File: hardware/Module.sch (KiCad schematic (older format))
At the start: 92 parts, among them J1 Power, J10 Jack, J11 A I/O, J12 Debug, J13 A IFACE, J2 B IFACE, J3 B I/O, J4 Jack, J5 Jack, J6 Jack, J7 Jack, J8 Jack, J9 Jack, SW2 Button, U1 MCP6004, U4 LM4040C10, U6 TL072, U9 MCP6002

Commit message: Prepare the schematic
Signed-off-by: Petr Horacek <hrck@protonmail.com>
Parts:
- removed C35, C37: 1n, Capacitor_SMD:C_0603_1608Metric_Pad1.08x0.95mm_HandSolder, symbol Device:C_Small
- removed D10, D3, D4, D5, D6, D7, D8, D9: LED, LED_THT:LED_D3.0mm, symbol Device:LED_Small
- removed J11: A I/O, Connector_PinHeader_2.54mm:PinHeader_2x06_P2.54mm_Vertical, symbol Connector_Generic:Conn_02x06_Odd_Even
- removed J13: A IFACE, Connector_PinHeader_2.54mm:PinHeader_2x08_P2.54mm_Vertical, symbol Connector_Generic:Conn_02x08_Odd_Even
- removed J2: B IFACE, Connector_PinSocket_2.54mm:PinSocket_2x08_P2.54mm_Vertical, symbol Connector_Generic:Conn_02x08_Odd_Even
- removed J3: B I/O, Connector_PinSocket_2.54mm:PinSocket_2x06_P2.54mm_Vertical, symbol Connector_Generic:Conn_02x06_Odd_Even
- removed R36, R37, R40, R41: 1k, Resistor_SMD:R_0603_1608Metric_Pad0.98x0.95mm_HandSolder, symbol Device:R_Small
- removed R50, R51: 47k, Resistor_SMD:R_0603_1608Metric_Pad0.98x0.95mm_HandSolder, symbol Device:R_Small
- removed RV1, RV2, RV3, RV4: B10k, Potentiometer_THT:Potentiometer_Alpha_RD901F-40-00D_Single_Vertical, symbol Device:R_POT
- removed SW2: Button, Button_Switch_THT:SW_PUSH_6mm, symbol Switch:SW_Push
- removed U6: TL072, Package_SO:SOIC-8_3.9x4.9mm_P1.27mm, symbol Amplifier_Operational:TL072
- added C1, C6, C7, C8, C9: 100n, Capacitor_SMD:C_0603_1608Metric_Pad1.08x0.95mm_HandSolder, symbol Device:C_Small
- added C2, C3: 18p, Capacitor_SMD:C_0603_1608Metric_Pad1.08x0.95mm_HandSolder, symbol Device:C_Small
- added D1: Schottky, Diode_SMD:D_SOD-123, symbol Device:D_Schottky_Small
- added J1, J4: Jack, symbol Connector:AudioJack3
- added J10, J5, J6, J7, J8, J9: Jack, Connector_Audio:Jack_3.5mm_QingPu_WQP-PJ398SM_Vertical_CircularHoles, symbol Connector:AudioJack2_SwitchT
- added J13: Micro_SD, symbol Connector:Micro_SD_Card
- added J2: OLED, symbol Connector_Generic:Conn_01x04
- added R1: 33R, Resistor_SMD:R_0603_1608Metric_Pad0.98x0.95mm_HandSolder, symbol Device:R_Small
- added R10, R14, R15, R20, R21, R26, R27, R28, R29: 100k, Resistor_SMD:R_0603_1608Metric_Pad0.98x0.95mm_HandSolder, symbol Device:R_Small
- added R12, R13: 6k8, Resistor_SMD:R_0603_1608Metric_Pad0.98x0.95mm_HandSolder, symbol Device:R_Small
- added R16, R17: 200k, Resistor_SMD:R_0603_1608Metric_Pad0.98x0.95mm_HandSolder, symbol Device:R_Small
- added R18, R19, R34: 1k, Resistor_SMD:R_0603_1608Metric_Pad0.98x0.95mm_HandSolder, symbol Device:R_Small
- added R2: 220R, Resistor_SMD:R_0603_1608Metric_Pad0.98x0.95mm_HandSolder, symbol Device:R_Small
- added R22, R23, R24, R25, R8, R9: 33k, Resistor_SMD:R_0603_1608Metric_Pad0.98x0.95mm_HandSolder, symbol Device:R_Small
- added R3: 10R, Resistor_SMD:R_0603_1608Metric_Pad0.98x0.95mm_HandSolder, symbol Device:R_Small
- added R32, R33: 100R, Resistor_SMD:R_0603_1608Metric_Pad0.98x0.95mm_HandSolder, symbol Device:R_Small
- added R43, R44, R6: 47k, Resistor_SMD:R_0603_1608Metric_Pad0.98x0.95mm_HandSolder, symbol Device:R_Small
- added R47, R5: 10k, Resistor_SMD:R_0603_1608Metric_Pad0.98x0.95mm_HandSolder, symbol Device:R_Small
- added SW1, SW2: Encoder, Rotary_Encoder:RotaryEncoder_Alps_EC11E-Switch_Vertical_H20mm, symbol Device:Rotary_Encoder_Switch
- added U1, U2, U3: TL074, symbol Amplifier_Operational:TL074
- R11: value 2k2 -> 100k
- R35: LCSC C23032 -> C21190; Mfr Part Number CR0603-FX-3650ELF -> CR0603-FX-1001ELF
- R38, R39, R42: value 1k -> 47k; LCSC C23032 -> C25744; Mfr Part Number CR0603-FX-3650ELF -> CR0603-FX-1002ELF
- R48: renamed from R20; value 100k -> 200k
- R52: renamed from R23; value 100k -> 200k
- R59: renamed from R17; value 100k -> 200k
- R7: value 2k2 -> 47k
- renumbered C33 to C10, C34 to C11, C41 to C12, C43 to C13, C44 to C14, C46 to C15, C48 to C16, C40 to C17, C42 to C18, C38 to C4, C36 to C5, D11 to D2, D1 to D3, D2 to D4, J5 to J11, J4 to J12, J6 to J14, J8 to J15, J10 to J16, J1 to J17, J7 to J18, J9 to J19, J12 to J3, R12 to R30, R8 to R31, R13 to R36, R9 to R37, R48 to R4, R14 to R40, R10 to R41, R43 to R45, R21 to R49, R27 to R50, R28 to R51, R30 to R53, R22 to R54, R29 to R55, R31 to R56, R45 to R57, R47 to R58, R18 to R60, R24 to R61, R25 to R62, R4 to R63, R19 to R64, R26 to R65, R5 to R66, U1 to U4, U9 to U5, U9 to U6, U4 to U7
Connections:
- net A_LED4 is gone; now on net +3V3: R38.1
- net A_LED5 is gone; now on net +3V3: R39.1
- net A_LED8 is gone; now on net +3V3: R42.1
- net B_CV1_IN is gone; now on an unnamed net: R49.1
- net B_CV2_IN is gone; now on an unnamed net: R60.1
- net B_CV3_IN is gone; now on an unnamed net: R51.1
- net B_CV4_IN is gone; now on an unnamed net: R62.1
- net B_CV5_IN is gone; now on an unnamed net: R53.1
- net B_LED3 is gone; now on net SD_CMD: A1.6 (SDMMC1_CMD)
- net B_LED4 is gone; now on net SD_D0: A1.5 (SDMMC1_D0)
- net B_LED5 is gone; now on net SD_D1: A1.4 (SDMMC1_D1)
- net B_OUT1_MAIN is gone; now on an unnamed net: C5.1, R37.2
- net B_OUT2_MAIN is gone; now on an unnamed net: C4.1, R36.2
- net B_POT3 is gone; now on net DAC2: A1.30 (DAC1_OUT1)
- net B_POT4 is gone; now on net DAC1: A1.29 (DAC1_OUT2)
- net +3.3VA: now also R22.1, R24.1
- net +3V3: now also C1.1, J13.4 (VDD), J2.1 (Pin_1), R1.1, R43.1, R44.1, U1.6 (VDD)
- net DAC1: now also R11.1, R10.1; no longer A1.18 (AUDIO_OUT_L), R7.1
- net DAC2: no longer A1.19 (AUDIO_OUT_R), R11.1
- net GND: now also C1.2, C8.2, C9.1, J1.S, J10.S, J13.6 (VSS), J13.9 (SHIELD), J2.2 (Pin_2), J4.S, J5.S, J6.S, J7.S, J8.S, J9.S, SW1.C, SW1.S2, SW2.C, SW2.S2, U1.10 (+), U1.12 (+), U1.3 (+), U1.4 (GND), U1.5 (+), U2.10 (+), U2.12 (+), U2.3 (+), U2.5 (+), U3.10 (+), U3.12 (+), U3.3 (+), U3.5 (+); no longer A1.12 (I2C1_SCL), A1.13 (I2C1_SDA), A1.14 (USART1_TX), A1.15 (USART1_RX)
- net GPIO1: no longer A1.34 (SAI2_FS_B)
- net GPIO2: no longer A1.35 (SAI2_SCK_B)
- net GPIO3: no longer A1.36 (USB_HS_D_-)
- net GPIO4: no longer A1.37 (USB_HS_D_+)
- net VCC: now also C6.1, C8.1, U1.4 (V+), U2.4 (V+), U3.4 (V+)
- net VEE: now also C7.2, C9.2, U1.11 (V-), U2.11 (V-), U3.11 (V-)
- net AUDIO_IN1: now reaches A1.16 (AUDIO_IN_L)
- net AUDIO_IN1: now also R19.2
- net AUDIO_IN2: now reaches A1.17 (AUDIO_IN_R)
- net AUDIO_IN2: now also R18.2
- net ENC1_A: now reaches A1.31 (SAI2_MCLK_B)
- net ENC1_A: now also SW1.A
- net ENC1_B: now reaches A1.32 (SAI2_SD_B)
- net ENC1_B: now also SW1.B
- net ENC2_A: now reaches A1.33 (SAI2_SD_A)
- net ENC2_A: now also SW2.A
- net at R35.2: now also J10.T
- net SD_D1: now reaches R38.2
- net SD_D1: now also J13.8 (DAT1)
- net SD_D0: now reaches R39.2
- net SD_D0: now also J13.7 (DAT0)
- net SD_CMD: now reaches R42.2
- net SD_CMD: now also J13.3 (CMD)
- net at R7.2: now also C3.2, R13.1, U3.2 (-); no longer R31.1
- net at R11.2: now also R17.1, U2.2 (-); no longer R30.1
- net at J16.TN: now also R47.2; no longer R4.2
- net A_CV1_IN: no longer names the net of J14.T
- net A_CV2_IN: no longer names the net of J18.T
- net A_CV3_IN: no longer names the net of J15.T
- net A_CV4_IN: no longer names the net of J19.T
- net A_CV5_IN: no longer names the net of J16.T
- net A_LED1: no longer names the net of R35.1
- net A_LED1: now also R29.2, U2.7
- net A_OUT1_MAIN: no longer names the net of R41.1
- net A_OUT1_MAIN: now also U3.8
- net A_OUT2_MAIN: no longer names the net of R40.1
- net A_OUT2_MAIN: now also U3.14
- net A_PROBE renamed PROBE
- net PROBE: now also D2.3, R47.1, R5.1
- net B_BUTTON renamed ENC2_CLICK
- net ENC2_CLICK: now also SW2.S1
- net B_LED1 renamed ENC1_CLICK
- net ENC1_CLICK: now also SW1.S1
- net B_LED2 renamed SD_CK
- net SD_CK: now also J13.5 (CLK)
- net B_LED6 renamed SD_D2
- net SD_D2: now also J13.1 (DAT2), R44.2
- net B_LED7 renamed SD_D3
- net SD_D3: now also J13.2 (DAT3/CD), R43.2
- net B_LED8: no longer names the net of A1.1 (USB_HS_ID)
- net B_OUT1_FALL: no longer names the net of C4.2, R30.2, R36.1
- net B_OUT1_FALL: now also U3.13 (-)
- net B_OUT2_FALL: no longer names the net of C5.2, R31.2, R37.1
- net B_OUT2_FALL: now also U3.9 (-)
- net B_POT1 renamed MIDI_OUT
- net MIDI_OUT: now also R3.1
- net B_POT2 renamed MIDI_IN
- net MIDI_IN: now also U1.5 (VO)
- net B_PROBE: no longer names the net of A1.11 (SPI1_MOSI)
- net B_PROBE: no longer D2.3
- new net: J5.TN, R4.2
- new net: R14.2, R20.1, U1.1
- new net: R20.2, R26.1, U1.6 (-)
- new net: R26.2, R32.1, U1.7
- new net: J7.T, R32.2
- new net: J4.R, R1.2
- new net: J4.T, R3.2
- new net: R15.2, R21.1, U1.8
- new net: R21.2, R27.1, U1.13 (-)
- new net: R27.2, R33.1, U1.14
- new net: J8.T, R33.2
- new net: R15.1, R9.2, U1.9 (-)
- new net: R14.1, R8.2, U1.2 (-)
- new net: C6.2, C7.1
- new net: C2.1, R12.2, R18.1, U3.7
- new net: J5.T, R6.1
- new net: C2.2, R12.1, R6.2, U3.6 (-)
- new net: C3.1, R13.2, R19.1, U3.1
- new net: J6.T, R7.1
- new net: J6.TN, R5.2
- new net: R17.2, R25.1, U2.1
- new net: R24.2, R25.2, R29.1, U2.6 (-)
- new net: J9.T, R34.2
- new net: R28.2, R34.1, U2.14
- new net: R22.2, R23.2, R28.1, U2.13 (-)
- new net: R16.2, R23.1, U2.8
- new net: R10.2, R16.1, U2.9 (-)
- new net: J1.R, R2.1
- new net: D1.2 (A), J1.T, U1.3 (K)
- new net: D1.1 (K), R2.2, U1.1 (A)
- new net AUDIO_OUT1: A1.18 (AUDIO_OUT_L), R31.1
- new net AUDIO_OUT2: A1.19 (AUDIO_OUT_R), R30.1
- new net ENC2_B: A1.34 (SAI2_FS_B), SW2.B
- new net GATE1: R8.1
- new net GATE2: R9.1
- new net OLED_SCL: A1.12 (I2C1_SCL), J2.3 (Pin_3)
- new net OLED_SDA: A1.13 (I2C1_SDA), J2.4 (Pin_4)
- no-connect marks 9 -> 3
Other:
- note removed: "0.0 to 10.0"
- note removed: "Audio Output"
- note removed: "CV Input"
- note removed: "Core"
- note removed: "Display"
- note removed: "Power"
- note removed: "R17 to R31 should be 1% for best CV accuracy"
- note removed: "User Input"
- note removed: "compatibility version 0"
- moved on the sheet: C10, C11, C12, C13, C14, C15, C16, C17, C18, C19, C20, C21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

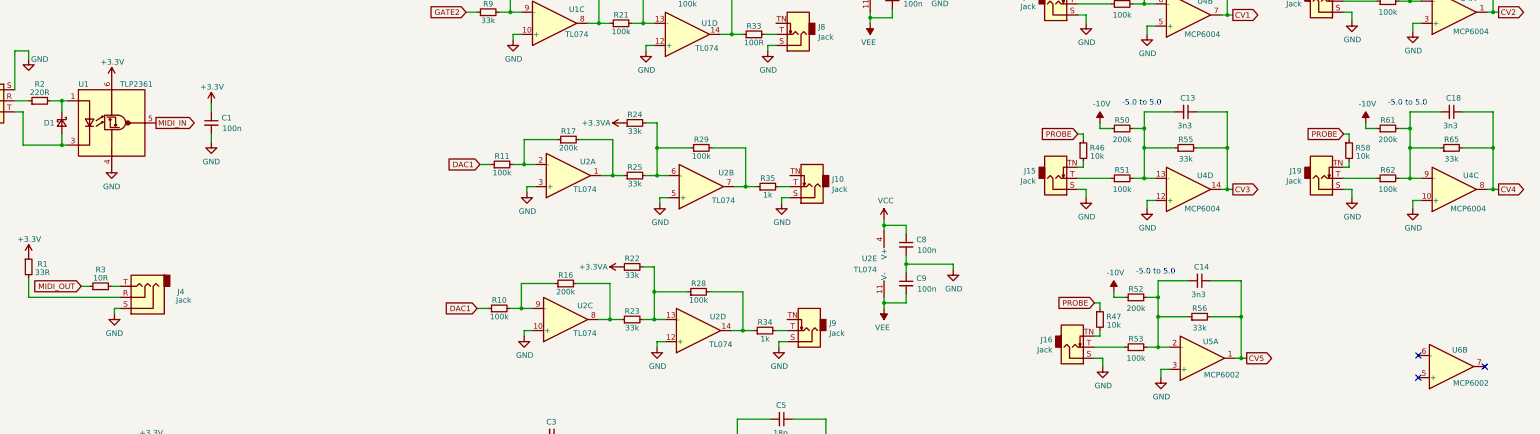
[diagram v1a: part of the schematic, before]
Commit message: Add SD card footprint
Signed-off-by: Petr Horacek <hrck@protonmail.com>
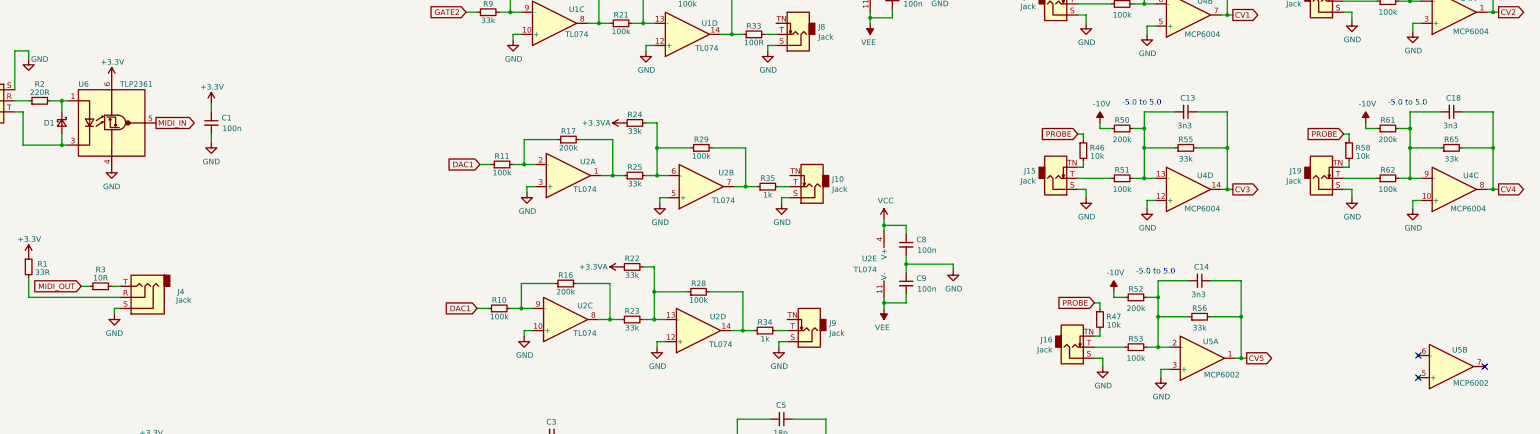
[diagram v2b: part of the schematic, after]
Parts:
- J1, J4: footprint (none) -> Connector_Audio:Jack_3.5mm_QingPu_WQP-PJ398SM_Vertical_CircularHoles
- J13: footprint (none) -> Custom:microsd_connector
- J2: footprint (none) -> Connector_PinHeader_2.54mm:PinHeader_1x04_P2.54mm_Vertical
- U1, U2, U3: footprint (none) -> Package_SO:SOIC-14_3.9x8.7mm_P1.27mm
- renumbered U6 to U5, U1 to U6
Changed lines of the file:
@@
 NoConn ~ 14825 8000
 $Comp
-L Amplifier_Operational:MCP6002-xSN U6
+L Amplifier_Operational:MCP6002-xSN U5
 U 2 1 62469350
 P 15125 7900
-F 0 "U6" H 15200 7750 50  0000 C CNN
+F 0 "U5" H 15200 7750 50  0000 C CNN
 F 1 "MCP6002" H 15300 8050 50  0000 C CNN
 F 2 "Package_SO:SOIC-8_3.9x4.9mm_P1.27mm" H 15125 7900 50  0001 C CNN
@@
 F 0 "J13" H 11125 2667 50  0000 C CNN
 F 1 "Micro_SD" H 11125 2576 50  0000 C CNN
-F 2 "" H 12325 2250 50  0001 C CNN
+F 2 "Custom:microsd_connector" H 12325 2250 50  0001 C CNN
 F 3 "http://katalog.we-online.de/em/datasheet/693072010801.pdf" H 11175 1950 50  0001 C CNN
 	1    11175 1950
@@
 F 0 "U1" H 7225 4675 50  0000 C CNN
 F 1 "TL074" H 7225 4900 50  0000 C CNN
-F 2 "" H 6975 4900 50  0001 C CNN
+F 2 "Package_SO:SOIC-14_3.9x8.7mm_P1.27mm" H 6975 4900 50  0001 C CNN
 F 3 "http://www.ti.com/lit/ds/symlink/tl071.pdf" H 7075 5000 50  0001 C CNN
 	3    7025 4800
@@
 F 0 "U1" H 8425 4800 50  0000 C CNN
 F 1 "TL074" H 8400 5025 50  0000 C CNN
-F 2 "" H 8175 5000 50  0001 C CNN
+F 2 "Package_SO:SOIC-14_3.9x8.7mm_P1.27mm" H 8175 5000 50  0001 C CNN
 F 3 "http://www.ti.com/lit/ds/symlink/tl071.pdf" H 8275 5100 50  0001 C CNN
 	4    8225 4900
@@
 F 0 "U1" H 9675 4450 50  0000 L CNN
 F 1 "TL074" H 9600 4350 50  0000 L CNN
-F 2 "" H 9925 4500 50  0001 C CNN
+F 2 "Package_SO:SOIC-14_3.9x8.7mm_P1.27mm" H 9925 4500 50  0001 C CNN
 F 3 "http://www.ti.com/lit/ds/symlink/tl071.pdf" H 10025 4600 50  0001 C CNN
 	5    9975 4400
@@
 F 0 "U1" H 7200 3700 50  0000 C CNN
 F 1 "TL074" H 7175 3950 50  0000 C CNN
-F 2 "" H 6975 3925 50  0001 C CNN
+F 2 "Package_SO:SOIC-14_3.9x8.7mm_P1.27mm" H 6975 3925 50  0001 C CNN
 F 3 "http://www.ti.com/lit/ds/symlink/tl071.pdf" H 7075 4025 50  0001 C CNN
 	1    7025 3825
@@
 F 0 "U1" H 8450 3800 50  0000 C CNN
 F 1 "TL074" H 8425 4050 50  0000 C CNN
-F 2 "" H 8175 4025 50  0001 C CNN
+F 2 "Package_SO:SOIC-14_3.9x8.7mm_P1.27mm" H 8175 4025 50  0001 C CNN
 F 3 "http://www.ti.com/lit/ds/symlink/tl071.pdf" H 8275 4125 50  0001 C CNN
 	2    8225 3925
@@
 F 0 "U3" H 7200 9075 50  0000 C CNN
 F 1 "TL074" H 7225 9300 50  0000 C CNN
-F 2 "" H 6950 9300 50  0001 C CNN
+F 2 "Package_SO:SOIC-14_3.9x8.7mm_P1.27mm" H 6950 9300 50  0001 C CNN
 F 3 "http://www.ti.com/lit/ds/symlink/tl071.pdf" H 7050 9400 50  0001 C CNN
 	1    7000 9200
@@
 F 0 "U3" H 7150 10475 50  0000 C CNN
 F 1 "TL074" H 7175 10700 50  0000 C CNN
-F 2 "" H 6925 10675 50  0001 C CNN
+F 2 "Package_SO:SOIC-14_3.9x8.7mm_P1.27mm" H 6925 10675 50  0001 C CNN
 F 3 "http://www.ti.com/lit/ds/symlink/tl071.pdf" H 7025 10775 50  0001 C CNN
 	2    6975 10575
@@
 F 0 "U3" H 9250 8925 50  0000 C CNN
 F 1 "TL074" H 9250 9175 50  0000 C CNN
-F 2 "" H 9025 9150 50  0001 C CNN
+F 2 "Package_SO:SOIC-14_3.9x8.7mm_P1.27mm" H 9025 9150 50  0001 C CNN
 F 3 "http://www.ti.com/lit/ds/symlink/tl071.pdf" H 9125 9250 50  0001 C CNN
 	3    9075 9050
@@
 F 0 "U3" H 9175 10325 50  0000 C CNN
 F 1 "TL074" H 9200 10575 50  0000 C CNN
-F 2 "" H 8950 10550 50  0001 C CNN
+F 2 "Package_SO:SOIC-14_3.9x8.7mm_P1.27mm" H 8950 10550 50  0001 C CNN
 F 3 "http://www.ti.com/lit/ds/symlink/tl071.pdf" H 9050 10650 50  0001 C CNN
 	4    9000 10450
@@
 F 0 "U3" H 10400 9825 50  0000 L CNN
 F 1 "TL074" H 10325 9725 50  0000 L CNN
-F 2 "" H 10650 9875 50  0001 C CNN
+F 2 "Package_SO:SOIC-14_3.9x8.7mm_P1.27mm" H 10650 9875 50  0001 C CNN
 F 3 "http://www.ti.com/lit/ds/symlink/tl071.pdf" H 10750 9975 50  0001 C CNN
 	5    10700 9775
@@
 F 0 "U2" H 8575 6150 50  0000 C CNN
 F 1 "TL074" H 8550 6400 50  0000 C CNN
-F 2 "" H 8300 6375 50  0001 C CNN
+F 2 "Package_SO:SOIC-14_3.9x8.7mm_P1.27mm" H 8300 6375 50  0001 C CNN
 F 3 "http://www.ti.com/lit/ds/symlink/tl071.pdf" H 8400 6475 50  0001 C CNN
 	2    8350 6275
@@
 F 0 "U2" H 7325 6050 50  0000 C CNN
 F 1 "TL074" H 7300 6300 50  0000 C CNN
-F 2 "" H 7100 6275 50  0001 C CNN
+F 2 "Package_SO:SOIC-14_3.9x8.7mm_P1.27mm" H 7100 6275 50  0001 C CNN
 F 3 "http://www.ti.com/lit/ds/symlink/tl071.pdf" H 7200 6375 50  0001 C CNN
 	1    7150 6175
@@
 F 0 "U2" H 9800 7025 50  0000 L CNN
 F 1 "TL074" H 9725 6925 50  0000 L CNN
-F 2 "" H 10050 7075 50  0001 C CNN
+F 2 "Package_SO:SOIC-14_3.9x8.7mm_P1.27mm" H 10050 7075 50  0001 C CNN
 F 3 "http://www.ti.com/lit/ds/symlink/tl071.pdf" H 10150 7175 50  0001 C CNN
 	5    10100 6975
@@
 F 0 "U2" H 7300 7350 50  0000 C CNN
 F 1 "TL074" H 7300 7600 50  0000 C CNN
-F 2 "" H 7075 7575 50  0001 C CNN
+F 2 "Package_SO:SOIC-14_3.9x8.7mm_P1.27mm" H 7075 7575 50  0001 C CNN
 F 3 "http://www.ti.com/lit/ds/symlink/tl071.pdf" H 7175 7675 50  0001 C CNN
 	3    7125 7475
@@
 F 0 "U2" H 8500 7450 50  0000 C CNN
 F 1 "TL074" H 8525 7700 50  0000 C CNN
-F 2 "" H 8275 7675 50  0001 C CNN
+F 2 "Package_SO:SOIC-14_3.9x8.7mm_P1.27mm" H 8275 7675 50  0001 C CNN
 F 3 "http://www.ti.com/lit/ds/symlink/tl071.pdf" H 8375 7775 50  0001 C CNN
 	4    8325 7575
@@
 F 0 "J1" H 1575 5575 50  0000 C CNN
 F 1 "Jack" H 1550 5500 50  0000 C CNN
-F 2 "" H 1950 5500 50  0001 C CNN
+F 2 "Connector_Audio:Jack_3.5mm_QingPu_WQP-PJ398SM_Vertical_CircularHoles" H 1950 5500 50  0001 C CNN
 F 3 "~" H 1950 5500 50  0001 C CNN
 	1    1950 5500
@@
 $EndComp
 $Comp
-L Isolator:TLP2761 U1
+L Isolator:TLP2761 U6
 U 1 1 644A7BD8
 P 3025 5700
-F 0 "U1" H 2725 6050 50  0000 L CNN
+F 0 "U6" H 2725 6050 50  0000 L CNN
 F 1 "TLP2361" H 3100 6050 50  0000 L CNN
 F 2 "Package_SO:SO-6L_10x3.84mm_P1.27mm" H 2325 5200 50  0001 L CIN
@@
 F 0 "J4" H 2950 7225 50  0000 C CNN
 F 1 "Jack" H 2925 7300 50  0000 C CNN
-F 2 "" H 3300 7275 50  0001 C CNN
+F 2 "Connector_Audio:Jack_3.5mm_QingPu_WQP-PJ398SM_Vertical_CircularHoles" H 3300 7275 50  0001 C CNN
 F 3 "~" H 3300 7275 50  0001 C CNN
 	1    3300 7275
@@
 F 0 "J2" H 2750 8875 50  0000 C CNN
 F 1 "OLED" H 2800 8775 50  0000 C CNN
-F 2 "" H 2625 8850 50  0001 C CNN
+F 2 "Connector_PinHeader_2.54mm:PinHeader_1x04_P2.54mm_Vertical" H 2625 8850 50  0001 C CNN
 F 3 "~" H 2625 8850 50  0001 C CNN
 	1    2625 8850

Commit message: Design the PCB
Signed-off-by: Petr Horacek <hrck@protonmail.com>
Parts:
- removed J2: OLED, Connector_PinHeader_2.54mm:PinHeader_1x04_P2.54mm_Vertical, symbol Connector_Generic:Conn_01x04
- removed J3: Debug, Connector_PinHeader_2.54mm:PinHeader_1x05_P2.54mm_Vertical, symbol Connector_Generic:Conn_01x05
- added J2: OLED, Connector_PinSocket_2.54mm:PinSocket_1x07_P2.54mm_Vertical, symbol Connector_Generic:Conn_01x07
- J1, J4: footprint Connector_Audio:Jack_3.5mm_QingPu_WQP-PJ398SM_Vertical_CircularHoles -> Custom:Jack_3.5mm_QingPu_WQP-PJ398SM_Vertical_CircularHoles_Stereo
- J17: footprint Connector_IDC:IDC-Header_2x05_P2.54mm_Vertical -> Connector_PinHeader_2.54mm:PinHeader_2x05_P2.54mm_Vertical
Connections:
- net OLED_SDA is gone; now on net ENC2_CLICK: A1.13 (I2C1_SDA)
- net +3V3: now also J2.2 (Pin_2)
- net AUDIO_IN1: now also A1.17 (AUDIO_IN_R); no longer A1.16 (AUDIO_IN_L)
- net AUDIO_IN2: now also A1.16 (AUDIO_IN_L); no longer A1.17 (AUDIO_IN_R)
- net CV1: now also A1.22 (ADC_INP10), C14.1, R56.2, U5.1; no longer A1.24 (ADC_INP5), C12.1, R54.2, U4.7
- net CV2: now also A1.24 (ADC_INP5); no longer A1.23 (ADC_INP15)
- net CV3: now also A1.25 (ADC_INP7); no longer A1.26 (ADC_INP3)
- net CV4: now also A1.26 (ADC_INP3); no longer A1.25 (ADC_INP7)
- net CV5: now also A1.23 (ADC_INP15), C12.1, R54.2, U4.7; no longer A1.22 (ADC_INP10), C14.1, R56.2, U5.1
- net DAC1: no longer R10.1
- net DAC2: now also R10.1
- net ENC1_A: now also A1.28 (ADC1_INP4); no longer A1.31 (SAI2_MCLK_B)
- net ENC1_B: now also A1.31 (SAI2_MCLK_B); no longer A1.32 (SAI2_SD_B)
- net ENC1_CLICK: now also A1.27 (ADC_INP11); no longer A1.8 (SPI1_NSS)
- net ENC2_A: now also A1.15 (USART1_RX); no longer A1.33 (SAI2_SD_A)
- net ENC2_B: now also A1.14 (USART1_TX); no longer A1.34 (SAI2_FS_B)
- net ENC2_CLICK: no longer A1.9 (SPI1_SCK)
- net GATE1: now also A1.34 (SAI2_FS_B)
- net GATE2: now also A1.35 (SAI2_SCK_B)
- net GND: now also C6.2, C7.1, J2.1 (Pin_1)
- net MIDI_IN: now also A1.32 (SAI2_SD_B); no longer A1.28 (ADC1_INP4)
- net MIDI_OUT: now also A1.33 (SAI2_SD_A); no longer A1.27 (ADC_INP11)
- net at J16.T: now also R62.1; no longer R53.1
- net at J16.TN: now also R45.2; no longer R47.2
- net at J15.T: now also R60.1; no longer R51.1
- net at J19.T: now also R51.1; no longer R62.1
- net at J18.T: now also R49.1; no longer R60.1
- net at J14.T: now also R53.1; no longer R49.1
- net at J14.TN: now also R47.2; no longer R45.2
- net OLED_CMD: now reaches A1.10 (SPI1_MISO)
- net OLED_CMD: now also J2.4 (Pin_4)
- net OLED_DATA: now reaches A1.11 (SPI1_MOSI)
- net OLED_DATA: now also J2.6 (Pin_6)
- net OLED_RST: now reaches A1.37 (USB_HS_D_+)
- net OLED_RST: now also J2.5 (Pin_5)
- net OLED_SCL: no longer names the net of A1.12 (I2C1_SCL)
- new net OLED_CS: A1.8 (SPI1_NSS), J2.3 (Pin_3)
- new net OLED_SCK: A1.9 (SPI1_SCK), J2.7 (Pin_7)
- no-connect marks 3 -> 12
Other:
- moved on the sheet: J14, J15, J16, J18, J19, J4, R1, R3, R45, R46, R57, R58
